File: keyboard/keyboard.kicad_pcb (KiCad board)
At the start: 2 copper layers, 319.5 x 106 mm, 145 parts, among them J1 USB_C_Receptacle, J4 ISP, SW1 RESET, U1 ATmega32U4-A, Y1 16MHz

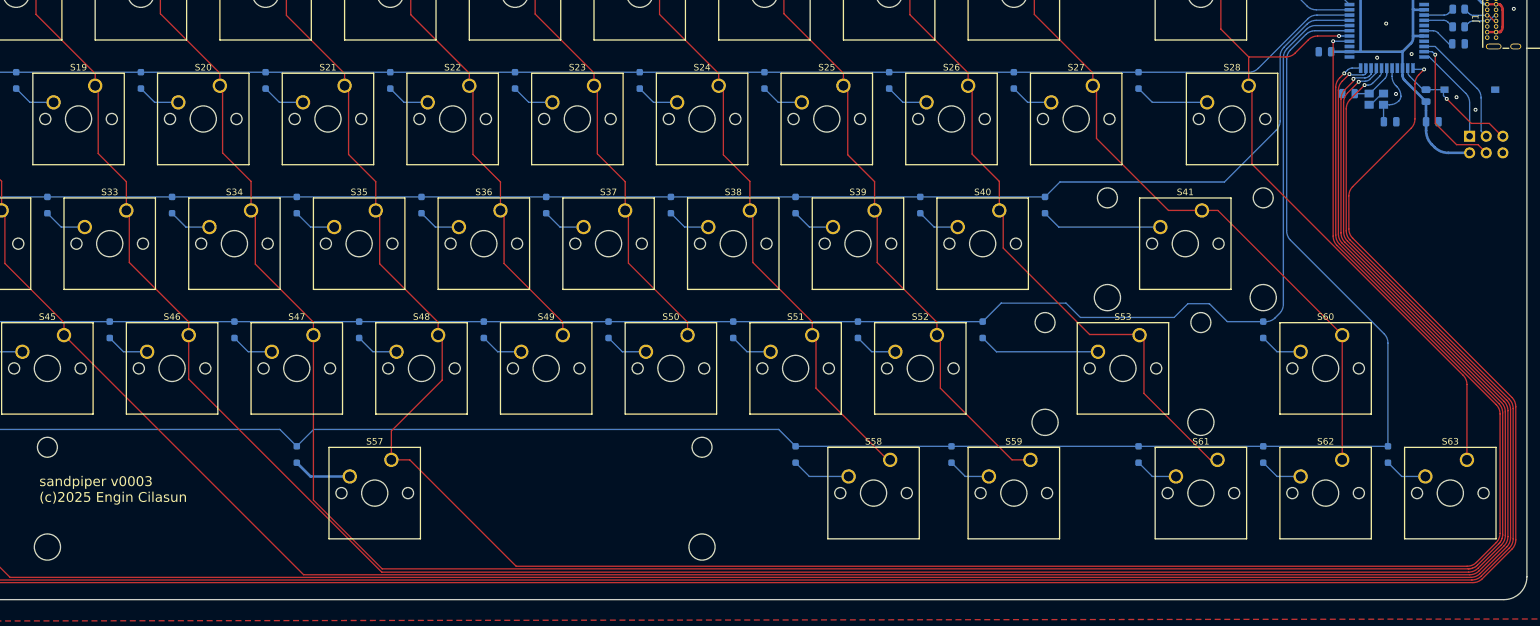
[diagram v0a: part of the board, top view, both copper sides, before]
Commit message: More fixes to the keyboard pcb
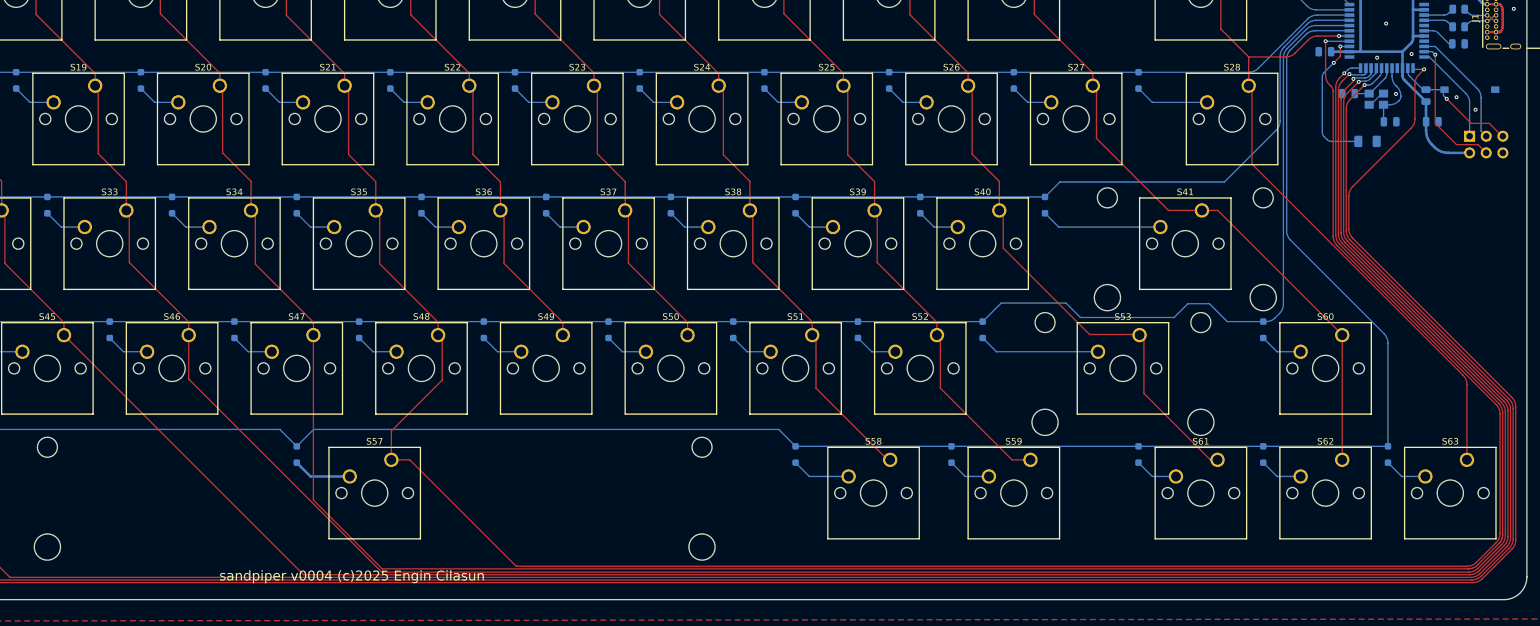
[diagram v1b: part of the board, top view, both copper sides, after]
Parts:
- added D64: LED_DEBUG, LED_SMD:LED_1206_3216Metric, B.Cu at (325.2, 61.2)
- R2, R3: value 22K -> 22R
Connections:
- U1 pad 25: unconnected-(U1-PD4-Pad25) -> Net-(D64-A)
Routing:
- net Net-(D64-A): track 0.00 -> 21.8 mm, vias 0 -> 2
- net Column 6: track 356.1 -> 357.5 mm
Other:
- board text added: "DEBUG"
- board text added: "sandpiper v0004 (c)2025 Engin Cilasun"
- board text removed: "ATmega32U4-A"
- board text removed: "sandpiper v0003 (c)2025 Engin Cilasun"

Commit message: Updated PCB layout, added caps
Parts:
- D64: value LED_DEBUG -> LED_READY
- S14: footprint sandpiperfootprints:SW_Cherry_MX_1.00u_PCB -> Button_Switch_Keyboard:SW_Cherry_MX_2.00u_PCB
- moved D64 29.4 mm to (338.5, 35.0)
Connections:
- U1 pad 1: unconnected-(U1-PE6-Pad1) -> Net-(D64-A)
- U1 pad 25: Net-(D64-A) -> unconnected-(U1-PD4-Pad25)
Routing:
- net Row 4: track 367.1 -> 74.0 mm
- net Row 3: track 318.2 -> 53.8 mm
- net Row 2: track 299.9 -> 63.2 mm
- net Net-(D64-A): track 21.8 -> 7.85 mm
- net GND: vias 7 -> 9
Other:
- board text added: "READY"
- board text removed: "DEBUG"

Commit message: New enclousre and fix for PCB
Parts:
- added J2: Conn_01x04_Pin, Connector_PinHeader_2.54mm:PinHeader_1x04_P2.54mm_Vertical, F.Cu at (345.6, 38.7)
- added REF**: MountingHole_2.2mm_M2, MountingHole:MountingHole_2.2mm_M2, F.Cu at (345.6, 127.0)
- added REF**: MountingHole_2.2mm_M2, MountingHole:MountingHole_2.2mm_M2, F.Cu at (34.0, 29.2)
- J1: moved to B.Cu
- moved J1 17.8 mm to (332.5, 31.4), turned to 0 degrees
- moved D64 14.6 mm to (326.0, 27.4), turned to 0 degrees
- moved SW1 6.05 mm to (339.0, 59.1), turned to 90 degrees
- moved J4 5.25 mm to (340.9, 65.7)
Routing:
- net USBD_P: track 5.48 -> 23.8 mm, vias 0 -> 1
- net USBD_N: track 5.49 -> 23.1 mm, vias 0 -> 1
- net RESET: track 20.7 -> 36.4 mm, vias 1 -> 0
- net Net-(D64-A): track 7.85 -> 18.6 mm
- net +5V: track 82.3 -> 92.9 mm
- net MISO: track 15.4 -> 20.7 mm
- net SCK: track 18.4 -> 23.3 mm
- net Column 5: track 364.8 -> 361.1 mm
- net Column 6: track 357.5 -> 353.8 mm
- net Column 4: track 374.6 -> 371.0 mm
- net Column 3: track 390.3 -> 386.7 mm
- net Column 2: track 431.2 -> 427.6 mm
- net Column 1: track 454.6 -> 451.0 mm
- net Column 0: track 475.3 -> 471.8 mm
- net MOSI: track 22.0 -> 24.9 mm, vias 1 -> 0
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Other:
- board text added: "5V0"
- board text added: "AVR ISP"
- board text added: "D+"
- board text added: "D-"
- board text added: "FPGAUSB:0"
- board text added: "FPGAUSB:1"
- board text added: "GND"
- board text removed: "AVRISP"
- board text removed: "READY"

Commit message: enclosure and pcb fixes
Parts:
- moved SW1 1.10 mm to (339.0, 58.0)
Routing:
- net Row 4: track 74.0 -> 365.4 mm
- net Row 3: track 53.8 -> 317.9 mm
- net Row 2: track 63.2 -> 298.9 mm
- net Row 0: track 293.2 -> 295.0 mm
- net RESET: track 36.4 -> 34.8 mm
- net Column 7: track 226.9 -> 227.6 mm
- net Column 8: track 206.9 -> 207.6 mm
- net Column 9: track 211.1 -> 211.7 mm
- net Column 10: track 193.4 -> 194.1 mm
- net Column 12: track 160.1 -> 160.7 mm
- net Column 11: track 180.7 -> 181.4 mm
